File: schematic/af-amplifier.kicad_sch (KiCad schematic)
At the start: 52 parts, among them J2 AudioJack3, Q5 2N3904, U15 NE5532, U7 TDA2003, U8 ADE-6

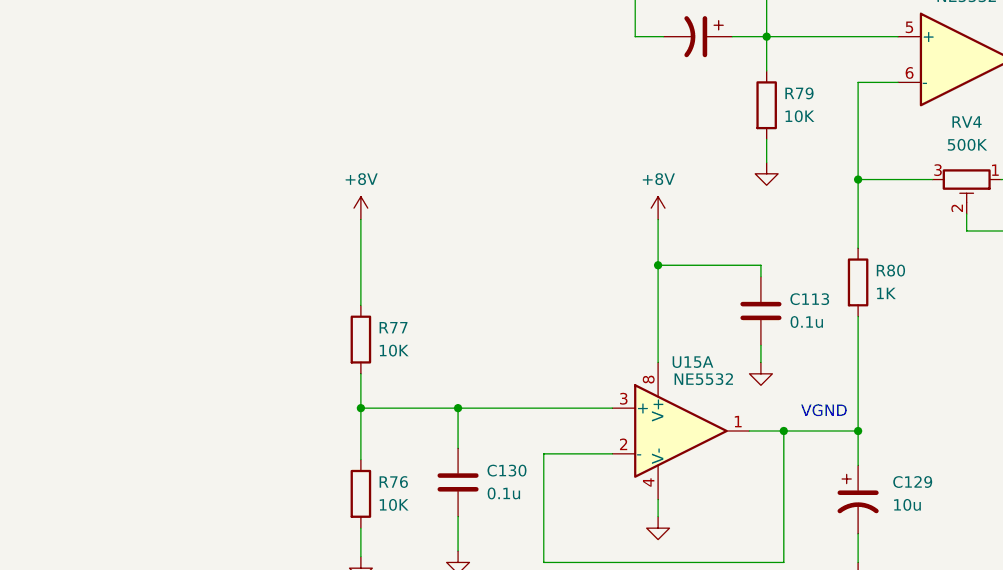
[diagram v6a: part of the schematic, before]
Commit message: Schematic: minor changes
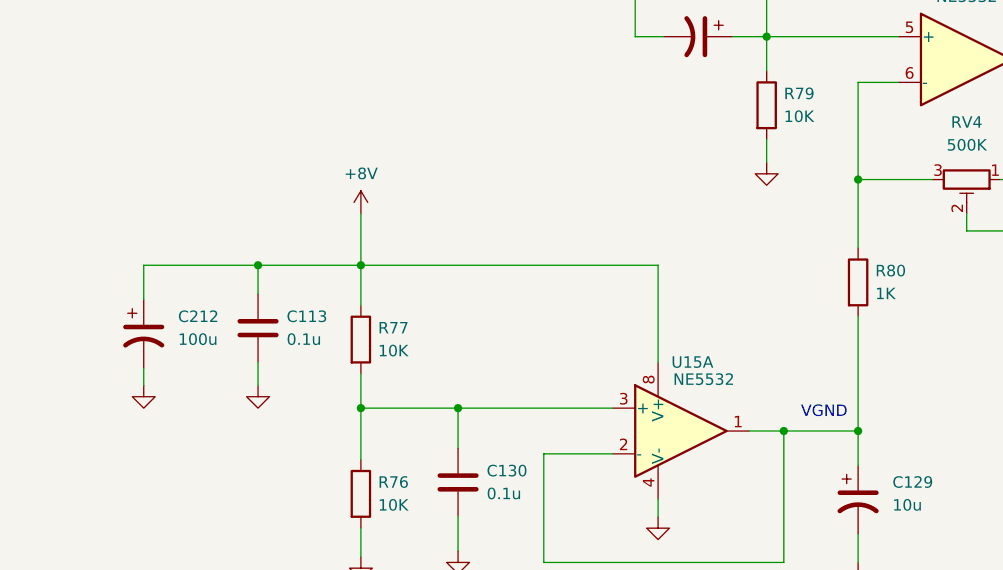
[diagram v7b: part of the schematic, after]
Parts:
- added C212: 100u, symbol Device:C_Polarized_US
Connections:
- net +8V: now also C212.1
- net GND: now also C212.2
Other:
- moved on the sheet: C113
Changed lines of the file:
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@@
   (junction (at 179.705 59.055) (diameter 0) (color 0 0 0 0)
   )
-  (junction (at 85.09 150.495) (diameter 0) (color 0 0 0 0)
+  (junction (at 40.64 150.495) (diameter 0) (color 0 0 0 0)
   )
   (junction (at 62.865 166.37) (diameter 0) (color 0 0 0 0)
@@
   (junction (at 125.73 140.97) (diameter 0) (color 0 0 0 0)
   )
+  (junction (at 52.07 150.495) (diameter 0) (color 0 0 0 0)
+  )
   (junction (at 229.87 61.595) (diameter 0) (color 0 0 0 0)
   )
@@
     (stroke (width 0) (type default))
   )
+  (wire (pts (xy 40.64 150.495) (xy 40.64 153.67))
+    (stroke (width 0) (type default))
+  )
   (wire (pts (xy 186.055 127.635) (xy 190.5 127.635))
     (stroke (width 0) (type default))
@@
     (stroke (width 0) (type default))
   )
-  (wire (pts (xy 85.09 150.495) (xy 96.52 150.495))
-    (stroke (width 0) (type default))
-  )
   (wire (pts (xy 243.205 86.36) (xy 243.205 76.2))
     (stroke (width 0) (type default))
@@
     (stroke (width 0) (type default))
   )
-  (wire (pts (xy 85.09 145.415) (xy 85.09 150.495))
+  (wire (pts (xy 52.07 144.78) (xy 52.07 150.495))
     (stroke (width 0) (type default))
   )
@@
     (stroke (width 0) (type default))
   )
+  (wire (pts (xy 40.64 150.495) (xy 52.07 150.495))
+    (stroke (width 0) (type default))
+  )
   (wire (pts (xy 220.98 38.735) (xy 220.98 36.195))
     (stroke (width 0) (type default))
@@
     (stroke (width 0) (type default))
   )
+  (wire (pts (xy 52.07 150.495) (xy 85.09 150.495))
+    (stroke (width 0) (type default))
+  )
   (wire (pts (xy 251.46 64.135) (xy 259.08 64.135))
     (stroke (width 0) (type default))
@@
     (stroke (width 0) (type default))
   )
+  (wire (pts (xy 27.94 161.925) (xy 27.94 163.83))
+    (stroke (width 0) (type default))
+  )
   (wire (pts (xy 73.66 67.945) (xy 73.66 72.39))
     (stroke (width 0) (type default))
@@
     (stroke (width 0) (type default))
   )
+  (wire (pts (xy 52.07 150.495) (xy 52.07 154.94))
+    (stroke (width 0) (type default))
+  )
   (wire (pts (xy 107.315 168.91) (xy 107.315 172.72))
     (stroke (width 0) (type default))
@@
     (stroke (width 0) (type default))
   )
+  (wire (pts (xy 27.94 154.305) (xy 27.94 150.495))
+    (stroke (width 0) (type default))
+  )
   (wire (pts (xy 131.445 127.635) (xy 134.62 127.635))
     (stroke (width 0) (type default))
@@
     (stroke (width 0) (type default))
   )
-  (wire (pts (xy 96.52 150.495) (xy 96.52 151.765))
-    (stroke (width 0) (type default))
-  )
   (wire (pts (xy 125.73 140.97) (xy 123.19 140.97))
     (stroke (width 0) (type default))
@@
     (stroke (width 0) (type default))
   )
-  (wire (pts (xy 52.07 145.415) (xy 52.07 154.94))
+  (wire (pts (xy 27.94 150.495) (xy 40.64 150.495))
     (stroke (width 0) (type default))
   )
@@
     (stroke (width 0) (type default))
   )
-  (wire (pts (xy 96.52 159.385) (xy 96.52 161.29))
+  (wire (pts (xy 40.64 161.29) (xy 40.64 163.83))
     (stroke (width 0) (type default))
   )
@@
         (path "/700c9878-4ed7-49d5-a273-77cf9d92989d/56e6206b-9eaf-48e3-8e65-5aed78d22a1d"
           (reference "R7") (unit 1)
+        )
+      )
+    )
+  )
+  (symbol (lib_id "power:GND") (at 27.94 163.83 0) (unit 1)
+    (in_bom yes) (on_board yes) (dnp no) (fields_autoplaced)
+    (property "Reference" "#PWR0240" (at 27.94 170.18 0)
+      (effects (font (size 1.27 1.27)) hide)
+    )
+    (property "Value" "GND" (at 27.94 168.91 0)
+      (effects (font (size 1.27 1.27)) hide)
+    )
+    (property "Footprint" "" (at 27.94 163.83 0)
+      (effects (font (size 1.27 1.27)) hide)
+    )
+    (property "Datasheet" "" (at 27.94 163.83 0)
+      (effects (font (size 1.27 1.27)) hide)
+    )
+    (pin "1")
+    (instances
+      (project "hbr-mk2"
+        (path "/700c9878-4ed7-49d5-a273-77cf9d92989d/56e6206b-9eaf-48e3-8e65-5aed78d22a1d"
+          (reference "#PWR0240") (unit 1)
         )
       )
@@
     )
   )
-  (symbol (lib_id "power:+8V") (at 85.09 145.415 0) (unit 1)
-    (in_bom yes) (on_board yes) (dnp no) (fields_autoplaced)
-    (property "Reference" "#PWR0240" (at 85.09 149.225 0)
-      (effects (font (size 1.27 1.27)) hide)
-    )
-    (property "Value" "+8V" (at 85.09 140.97 0)
-      (effects (font (size 1.27 1.27)))
-    )
-    (property "Footprint" "" (at 85.09 145.415 0)
-      (effects (font (size 1.27 1.27)) hide)
-    )
-    (property "Datasheet" "" (at 85.09 145.415 0)
+  (symbol (lib_id "power:+8V") (at 52.07 144.78 0) (unit 1)
+    (in_bom yes) (on_board yes) (dnp no) (fields_autoplaced)
+    (property "Reference" "#PWR0240" (at 52.07 148.59 0)
+      (effects (font (size 1.27 1.27)) hide)
+    )
+    (property "Value" "+8V" (at 52.07 140.335 0)
+      (effects (font (size 1.27 1.27)))
+    )
+    (property "Footprint" "" (at 52.07 144.78 0)
+      (effects (font (size 1.27 1.27)) hide)
+    )
+    (property "Datasheet" "" (at 52.07 144.78 0)
       (effects (font (size 1.27 1.27)) hide)
     )
@@
     )
   )
+  (symbol (lib_id "Device:C_Polarized_US") (at 27.94 158.115 0) (unit 1)
+    (in_bom yes) (on_board yes) (dnp no) (fields_autoplaced)
+    (property "Reference" "C212" (at 31.75 156.21 0)
+      (effects (font (size 1.27 1.27)) (justify left))
+    )
+    (property "Value" "100u" (at 31.75 158.75 0)
+      (effects (font (size 1.27 1.27)) (justify left))
+    )
+    (property "Footprint" "" (at 27.94 158.115 0)
+      (effects (font (size 1.27 1.27)) hide)
+    )
+    (property "Datasheet" "~" (at 27.94 158.115 0)
+      (effects (font (size 1.27 1.27)) hide)
+    )
+    (pin "1")
+    (pin "2")
+    (instances
+      (project "hbr-mk2"
+        (path "/700c9878-4ed7-49d5-a273-77cf9d92989d/56e6206b-9eaf-48e3-8e65-5aed78d22a1d"
+          (reference "C212") (unit 1)
+        )
+      )
+    )
+  )
   (symbol (lib_id "power:GND") (at 203.2 71.755 0) (unit 1)
     (in_bom yes) (on_board yes) (dnp no) (fields_autoplaced)
@@
     )
   )
-  (symbol (lib_id "Device:C") (at 96.52 155.575 0) (unit 1)
-    (in_bom yes) (on_board yes) (dnp no) (fields_autoplaced)
-    (property "Reference" "C113" (at 99.695 154.305 0)
-      (effects (font (size 1.27 1.27)) (justify left))
-    )
-    (property "Value" "0.1u" (at 99.695 156.845 0)
-      (effects (font (size 1.27 1.27)) (justify left))
-    )
-    (property "Footprint" "" (at 97.4852 159.385 0)
-      (effects (font (size 1.27 1.27)) hide)
-    )
-    (property "Datasheet" "~" (at 96.52 155.575 0)
+  (symbol (lib_id "Device:C") (at 40.64 157.48 0) (unit 1)
+    (in_bom yes) (on_board yes) (dnp no) (fields_autoplaced)
+    (property "Reference" "C113" (at 43.815 156.21 0)
+      (effects (font (size 1.27 1.27)) (justify left))
+    )
+    (property "Value" "0.1u" (at 43.815 158.75 0)
+      (effects (font (size 1.27 1.27)) (justify left))
+    )
+    (property "Footprint" "" (at 41.6052 161.29 0)
+      (effects (font (size 1.27 1.27)) hide)
+    )
+    (property "Datasheet" "~" (at 40.64 157.48 0)
       (effects (font (size 1.27 1.27)) hide)
     )
@@
     )
   )
-  (symbol (lib_id "power:GND") (at 96.52 161.29 0) (unit 1)
-    (in_bom yes) (on_board yes) (dnp no) (fields_autoplaced)
-    (property "Reference" "#PWR0219" (at 96.52 167.64 0)
-      (effects (font (size 1.27 1.27)) hide)
-    )
-    (property "Value" "GND" (at 96.52 166.37 0)
-      (effects (font (size 1.27 1.27)) hide)
-    )
-    (property "Footprint" "" (at 96.52 161.29 0)
-      (effects (font (size 1.27 1.27)) hide)
-    )
-    (property "Datasheet" "" (at 96.52 161.29 0)
+  (symbol (lib_id "power:GND") (at 40.64 163.83 0) (unit 1)
+    (in_bom yes) (on_board yes) (dnp no) (fields_autoplaced)
+    (property "Reference" "#PWR0219" (at 40.64 170.18 0)
+      (effects (font (size 1.27 1.27)) hide)
+    )
+    (property "Value" "GND" (at 40.64 168.91 0)
+      (effects (font (size 1.27 1.27)) hide)
+    )
+    (property "Footprint" "" (at 40.64 163.83 0)
+      (effects (font (size 1.27 1.27)) hide)
+    )
+    (property "Datasheet" "" (at 40.64 163.83 0)
       (effects (font (size 1.27 1.27)) hide)
     )
@@
         )
       )
-    )
-  )
-  (symbol (lib_id "power:+8V") (at 52.07 145.415 0) (unit 1)
-    (in_bom yes) (on_board yes) (dnp no) (fields_autoplaced)
-    (property "Reference" "#PWR0240" (at 52.07 149.225 0)
-      (effects (font (size 1.27 1.27)) hide)
-    )
-    (property "Value" "+8V" (at 52.07 140.97 0)
-      (effects (font (size 1.27 1.27)))
-    )
-    (property "Footprint" "" (at 52.07 145.415 0)
-      (effects (font (size 1.27 1.27)) hide)
-    )
-    (property "Datasheet" "" (at 52.07 145.415 0)
-      (effects (font (size 1.27 1.27)) hide)
-    )
-    (pin "1")
-    (instances
-      (project "hbr-mk2"
-        (path "/700c9878-4ed7-49d5-a273-77cf9d92989d/53c64ec8-e682-4447-a686-92e02593189c"
-          (reference "#PWR0240") (unit 1)
-        )
-        (path "/700c9878-4ed7-49d5-a273-77cf9d92989d/56e6206b-9eaf-48e3-8e65-5aed78d22a1d"
-          (reference "#PWR0240") (unit 1)
-        )
-      )
